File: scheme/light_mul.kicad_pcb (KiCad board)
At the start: 2 copper layers, 100 parts, among them J1 Screw_Terminal_01x04 (buttons), J2 Conn_01x06_Male (programmer), J3 Screw_Terminal_01x06 (output), J4 Conn_01x02_Male (i2c), J5 Conn_01x02_Male (Jumper), J6 Conn_01x03_Male (Indicators), J7 Screw_Terminal_01x02 (power), Q1 IRF8308M, Q2 IRF8308M, Q3 IRF8308M, SW1 SW_Push (reset), U1 L7805, U2 ATmega8A-PU

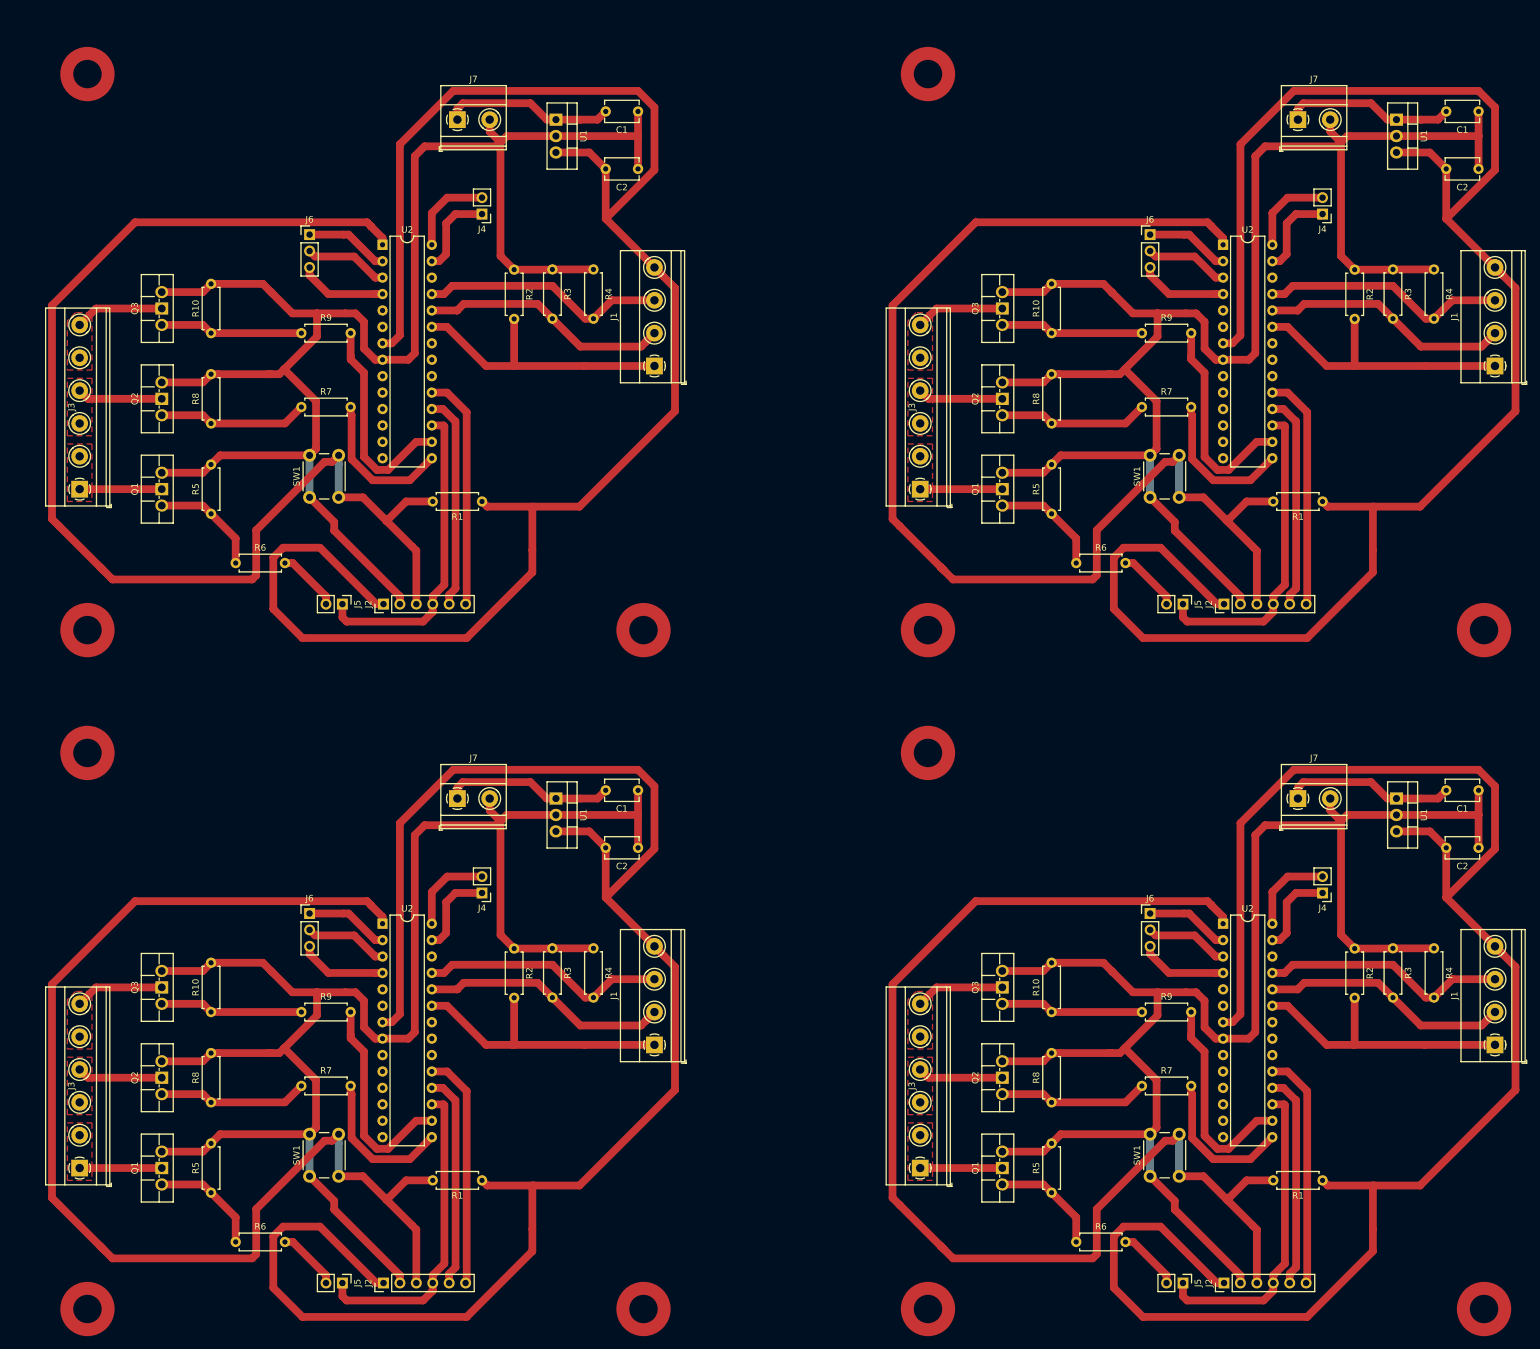
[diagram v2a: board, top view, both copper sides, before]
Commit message: cheme: add marks layer
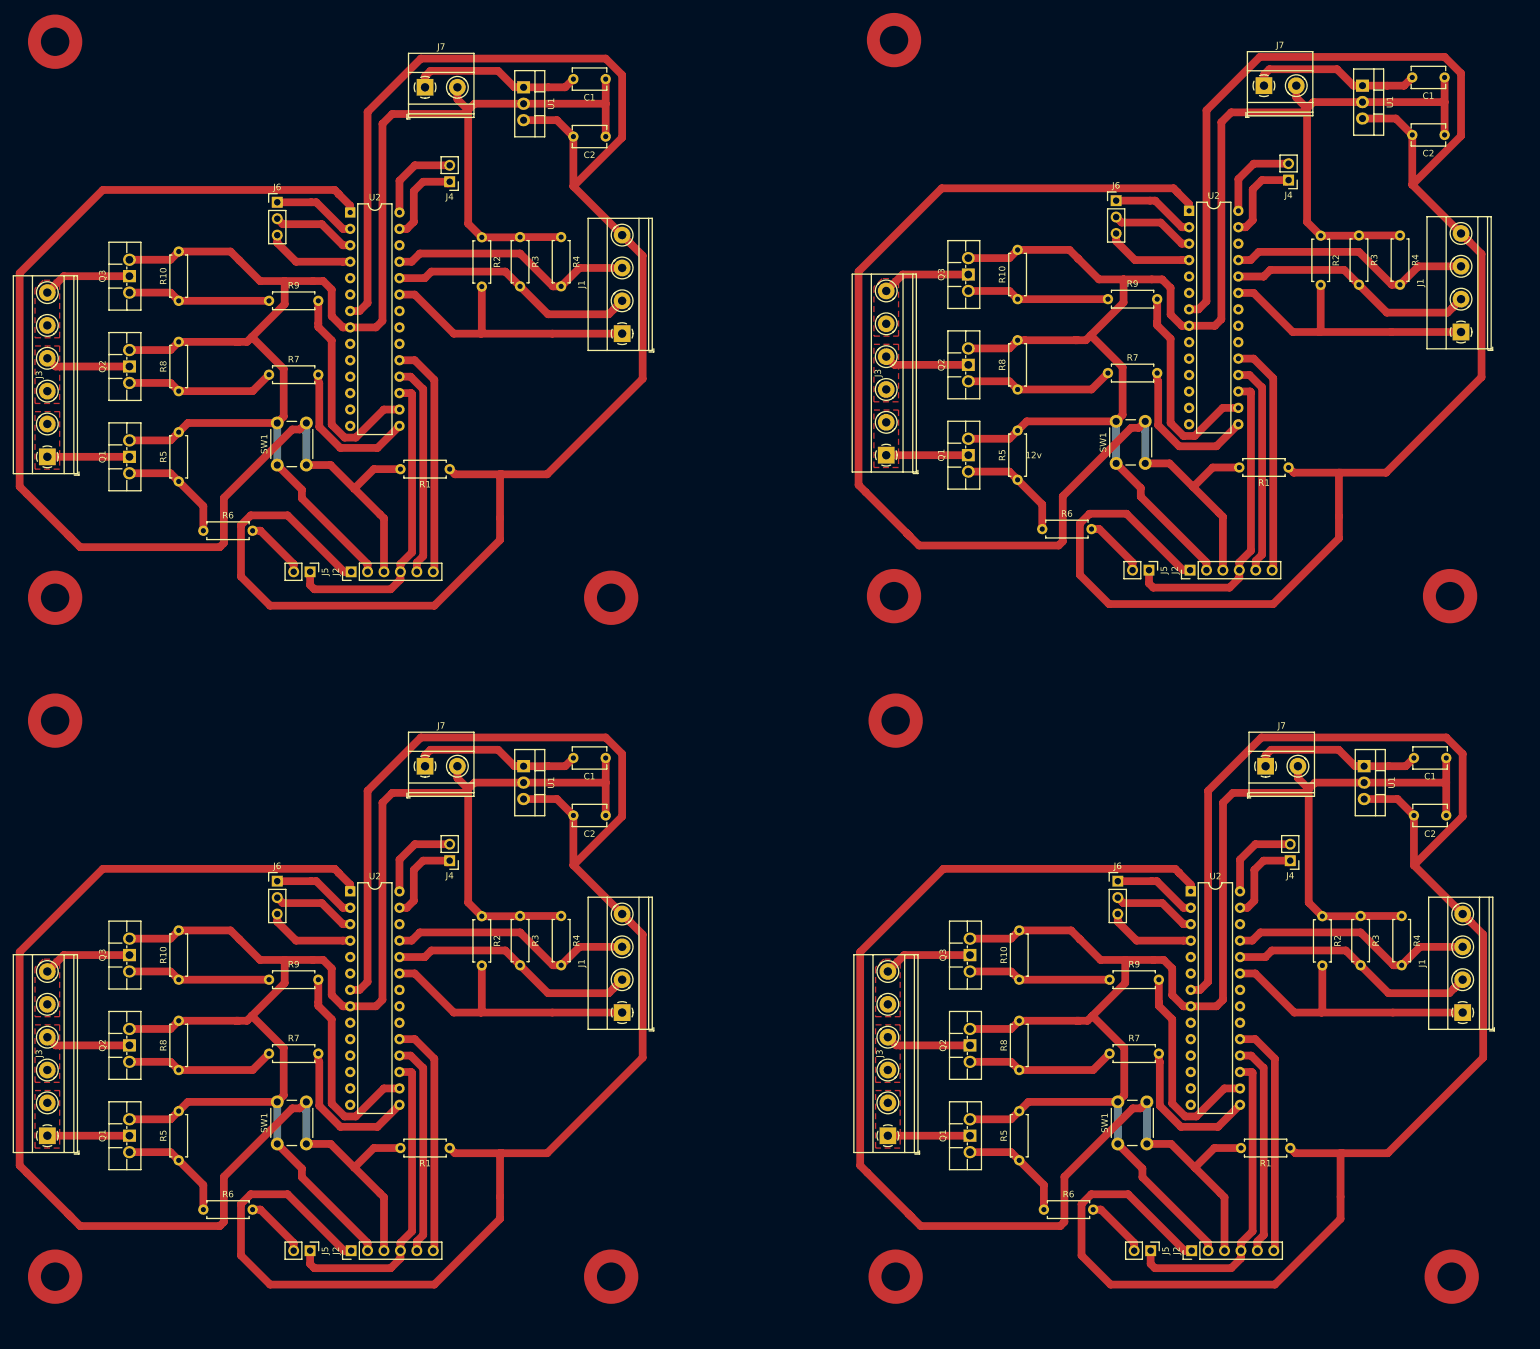
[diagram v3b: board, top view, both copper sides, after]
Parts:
- removed the C1 at (227.2, 122.8)
- removed the C1 at (227.2, 17.8)
- removed the C1 at (97.2, 122.8)
- removed the C2 at (227.2, 131.7)
- removed the C2 at (227.2, 26.7)
- removed the C2 at (97.2, 131.7)
- removed the J1 at (229.7, 162.2)
- removed the J1 at (229.7, 57.1)
- removed the J1 at (99.7, 162.2)
- removed the J2 at (187.8, 199.0)
- removed the J2 at (187.8, 94.0)
- removed the J2 at (57.8, 199.0)
- removed the J3 at (140.8, 181.2)
- removed the J3 at (140.8, 76.2)
- removed the J3 at (10.8, 181.2)
- removed the J4 at (203.0, 138.7)
- removed the J4 at (203.0, 33.7)
- removed the J4 at (73.0, 138.7)
- removed the J5 at (181.4, 199.0)
- removed the J5 at (181.4, 94.0)
- removed the J5 at (51.4, 199.0)
- removed the J6 at (176.4, 141.8)
- removed the J6 at (176.4, 36.8)
- removed the J6 at (46.4, 141.8)
- removed the J7 at (199.2, 124.0)
- removed the J7 at (199.2, 19.1)
- removed the J7 at (69.2, 124.0)
- removed the Q1 at (153.5, 183.7)
- removed the Q1 at (153.5, 78.7)
- removed the Q1 at (23.5, 183.7)
- removed the Q2 at (153.5, 169.8)
- removed the Q2 at (153.5, 64.8)
- removed the Q2 at (23.5, 169.8)
- removed the Q3 at (153.5, 155.8)
- removed the Q3 at (153.5, 50.8)
- removed the Q3 at (23.5, 155.8)
- removed the R1 at (203.0, 183.1)
- removed the R1 at (203.0, 78.1)
- removed the R1 at (73.0, 183.1)
- removed the R10 at (161.1, 157.1)
- removed the R10 at (161.1, 52.1)
- removed the R10 at (31.1, 157.1)
- removed the R2 at (208.0, 147.3)
- removed the R2 at (208.0, 42.3)
- removed the R2 at (78.0, 147.3)
- removed the R3 at (213.9, 147.2)
- removed the R3 at (213.9, 42.2)
- removed the R3 at (83.9, 147.2)
- removed the R4 at (220.3, 147.2)
- removed the R4 at (220.3, 42.2)
- removed the R4 at (90.3, 147.2)
- removed the R5 at (161.1, 185.0)
- removed the R5 at (161.1, 80.0)
- removed the R5 at (31.1, 185.0)
- removed the R6 at (164.9, 192.6)
- removed the R6 at (164.9, 87.6)
- removed the R6 at (34.9, 192.6)
- removed the R7 at (175.1, 168.5)
- removed the R7 at (175.1, 63.5)
- removed the R7 at (45.1, 168.5)
- removed the R8 at (161.1, 171.0)
- removed the R8 at (161.1, 66.0)
- removed the R8 at (31.1, 171.0)
- removed the R9 at (175.1, 157.1)
- removed the R9 at (175.1, 52.1)
- removed the R9 at (45.1, 157.1)
- removed the SW1 at (176.4, 182.5)
- removed the SW1 at (176.4, 77.5)
- removed the SW1 at (46.4, 182.5)
- removed the U1 at (214.5, 124.0)
- removed the U1 at (214.5, 19.1)
- removed the U1 at (84.5, 124.0)
- removed the U2 at (187.6, 143.4)
- removed the U2 at (187.6, 38.4)
- removed the U2 at (57.6, 143.4)
- added C1: 3.3uF, Capacitor_THT:C_Disc_D5.1mm_W3.2mm_P5.00mm, F.Cu at (222.2, 117.8)
- added C1: 3.3uF, Capacitor_THT:C_Disc_D5.1mm_W3.2mm_P5.00mm, F.Cu at (92.2, 117.8)
- added C1: 3.3uF, Capacitor_THT:C_Disc_D5.1mm_W3.2mm_P5.00mm, F.Cu at (221.9, 12.5)
- added C2: 0.1uF, Capacitor_THT:C_Disc_D5.1mm_W3.2mm_P5.00mm, F.Cu at (222.2, 126.7)
- added C2: 0.1uF, Capacitor_THT:C_Disc_D5.1mm_W3.2mm_P5.00mm, F.Cu at (92.2, 126.7)
- added C2: 0.1uF, Capacitor_THT:C_Disc_D5.1mm_W3.2mm_P5.00mm, F.Cu at (221.9, 21.4)
- added J1: Screw_Terminal_01x04 (buttons), TerminalBlock_Phoenix:TerminalBlock_Phoenix_MKDS-1,5-4-5.08_1x04_P5.08mm_Horizontal, F.Cu at (224.7, 157.2)
- added J1: Screw_Terminal_01x04 (buttons), TerminalBlock_Phoenix:TerminalBlock_Phoenix_MKDS-1,5-4-5.08_1x04_P5.08mm_Horizontal, F.Cu at (94.7, 157.2)
- added J1: Screw_Terminal_01x04 (buttons), TerminalBlock_Phoenix:TerminalBlock_Phoenix_MKDS-1,5-4-5.08_1x04_P5.08mm_Horizontal, F.Cu at (224.4, 51.9)
- added J2: Conn_01x06_Male (programmer), Connector_PinHeader_2.54mm:PinHeader_1x06_P2.54mm_Vertical, F.Cu at (182.8, 194.0)
- added J2: Conn_01x06_Male (programmer), Connector_PinHeader_2.54mm:PinHeader_1x06_P2.54mm_Vertical, F.Cu at (52.8, 194.0)
- added J2: Conn_01x06_Male (programmer), Connector_PinHeader_2.54mm:PinHeader_1x06_P2.54mm_Vertical, F.Cu at (182.5, 88.7)
- added J3: Screw_Terminal_01x06 (output), TerminalBlock_Phoenix:TerminalBlock_Phoenix_MKDS-1,5-6-5.08_1x06_P5.08mm_Horizontal, F.Cu at (135.8, 176.2)
- added J3: Screw_Terminal_01x06 (output), TerminalBlock_Phoenix:TerminalBlock_Phoenix_MKDS-1,5-6-5.08_1x06_P5.08mm_Horizontal, F.Cu at (5.79, 176.2)
- added J3: Screw_Terminal_01x06 (output), TerminalBlock_Phoenix:TerminalBlock_Phoenix_MKDS-1,5-6-5.08_1x06_P5.08mm_Horizontal, F.Cu at (135.5, 70.9)
- added J4: Conn_01x02_Male (i2c), Connector_PinHeader_2.54mm:PinHeader_1x02_P2.54mm_Vertical, F.Cu at (198.0, 133.7)
- added J4: Conn_01x02_Male (i2c), Connector_PinHeader_2.54mm:PinHeader_1x02_P2.54mm_Vertical, F.Cu at (68.0, 133.7)
- added J4: Conn_01x02_Male (i2c), Connector_PinHeader_2.54mm:PinHeader_1x02_P2.54mm_Vertical, F.Cu at (197.8, 28.4)
- added J5: Conn_01x02_Male (Jumper), Connector_PinHeader_2.54mm:PinHeader_1x02_P2.54mm_Vertical, F.Cu at (176.4, 194.0)
- added J5: Conn_01x02_Male (Jumper), Connector_PinHeader_2.54mm:PinHeader_1x02_P2.54mm_Vertical, F.Cu at (46.4, 194.0)
- added J5: Conn_01x02_Male (Jumper), Connector_PinHeader_2.54mm:PinHeader_1x02_P2.54mm_Vertical, F.Cu at (176.2, 88.7)
- added J6: Conn_01x03_Male (Indicators), Connector_PinHeader_2.54mm:PinHeader_1x03_P2.54mm_Vertical, F.Cu at (171.4, 136.8)
- added J6: Conn_01x03_Male (Indicators), Connector_PinHeader_2.54mm:PinHeader_1x03_P2.54mm_Vertical, F.Cu at (41.4, 136.8)
- added J6: Conn_01x03_Male (Indicators), Connector_PinHeader_2.54mm:PinHeader_1x03_P2.54mm_Vertical, F.Cu at (171.1, 31.6)
- added J7: Screw_Terminal_01x02 (power), TerminalBlock_Phoenix:TerminalBlock_Phoenix_MKDS-1,5-2_1x02_P5.00mm_Horizontal, F.Cu at (194.2, 119.0)
- added J7: Screw_Terminal_01x02 (power), TerminalBlock_Phoenix:TerminalBlock_Phoenix_MKDS-1,5-2_1x02_P5.00mm_Horizontal, F.Cu at (64.2, 119.0)
- added J7: Screw_Terminal_01x02 (power), TerminalBlock_Phoenix:TerminalBlock_Phoenix_MKDS-1,5-2_1x02_P5.00mm_Horizontal, F.Cu at (194.0, 13.8)
- added Q1: IRF8308M, scheme:IRF840, F.Cu at (148.5, 178.7)
- added Q1: IRF8308M, scheme:IRF840, F.Cu at (18.5, 178.7)
- added Q1: IRF8308M, scheme:IRF840, F.Cu at (148.2, 73.5)
- added Q2: IRF8308M, scheme:IRF840, F.Cu at (148.5, 164.8)
- added Q2: IRF8308M, scheme:IRF840, F.Cu at (18.5, 164.8)
- added Q2: IRF8308M, scheme:IRF840, F.Cu at (148.2, 59.5)
- added Q3: IRF8308M, scheme:IRF840, F.Cu at (148.5, 150.8)
- added Q3: IRF8308M, scheme:IRF840, F.Cu at (18.5, 150.8)
- added Q3: IRF8308M, scheme:IRF840, F.Cu at (148.2, 45.5)
- added R1: 10K, Resistor_THT:R_Axial_DIN0207_L6.3mm_D2.5mm_P7.62mm_Horizontal, F.Cu at (198.0, 178.1)
- added R1: 10K, Resistor_THT:R_Axial_DIN0207_L6.3mm_D2.5mm_P7.62mm_Horizontal, F.Cu at (68.0, 178.1)
- added R1: 10K, Resistor_THT:R_Axial_DIN0207_L6.3mm_D2.5mm_P7.62mm_Horizontal, F.Cu at (197.8, 72.9)
- added R10: 10K, Resistor_THT:R_Axial_DIN0207_L6.3mm_D2.5mm_P7.62mm_Horizontal, F.Cu at (156.1, 152.1)
- added R10: 10K, Resistor_THT:R_Axial_DIN0207_L6.3mm_D2.5mm_P7.62mm_Horizontal, F.Cu at (26.1, 152.1)
- added R10: 10K, Resistor_THT:R_Axial_DIN0207_L6.3mm_D2.5mm_P7.62mm_Horizontal, F.Cu at (155.9, 46.8)
- added R2: 220Ohm, Resistor_THT:R_Axial_DIN0207_L6.3mm_D2.5mm_P7.62mm_Horizontal, F.Cu at (203.0, 142.3)
- added R2: 220Ohm, Resistor_THT:R_Axial_DIN0207_L6.3mm_D2.5mm_P7.62mm_Horizontal, F.Cu at (73.0, 142.3)
- added R2: 220Ohm, Resistor_THT:R_Axial_DIN0207_L6.3mm_D2.5mm_P7.62mm_Horizontal, F.Cu at (202.7, 37.0)
- added R3: 220Ohm, Resistor_THT:R_Axial_DIN0207_L6.3mm_D2.5mm_P7.62mm_Horizontal, F.Cu at (208.9, 142.2)
- added R3: 220Ohm, Resistor_THT:R_Axial_DIN0207_L6.3mm_D2.5mm_P7.62mm_Horizontal, F.Cu at (78.9, 142.2)
- added R3: 220Ohm, Resistor_THT:R_Axial_DIN0207_L6.3mm_D2.5mm_P7.62mm_Horizontal, F.Cu at (208.7, 37.0)
- added R4: 220Ohm, Resistor_THT:R_Axial_DIN0207_L6.3mm_D2.5mm_P7.62mm_Horizontal, F.Cu at (215.3, 142.2)
- added R4: 220Ohm, Resistor_THT:R_Axial_DIN0207_L6.3mm_D2.5mm_P7.62mm_Horizontal, F.Cu at (85.3, 142.2)
- added R4: 220Ohm, Resistor_THT:R_Axial_DIN0207_L6.3mm_D2.5mm_P7.62mm_Horizontal, F.Cu at (215.0, 37.0)
- added R5: 10K, Resistor_THT:R_Axial_DIN0207_L6.3mm_D2.5mm_P7.62mm_Horizontal, F.Cu at (156.1, 180.0)
- added R5: 10K, Resistor_THT:R_Axial_DIN0207_L6.3mm_D2.5mm_P7.62mm_Horizontal, F.Cu at (26.1, 180.0)
- added R5: 10K, Resistor_THT:R_Axial_DIN0207_L6.3mm_D2.5mm_P7.62mm_Horizontal, F.Cu at (155.9, 74.8)
- added R6: 100Ohm, Resistor_THT:R_Axial_DIN0207_L6.3mm_D2.5mm_P7.62mm_Horizontal, F.Cu at (159.9, 187.6)
- added R6: 100Ohm, Resistor_THT:R_Axial_DIN0207_L6.3mm_D2.5mm_P7.62mm_Horizontal, F.Cu at (29.9, 187.6)
- added R6: 100Ohm, Resistor_THT:R_Axial_DIN0207_L6.3mm_D2.5mm_P7.62mm_Horizontal, F.Cu at (159.7, 82.4)
- added R7: 100Ohm, Resistor_THT:R_Axial_DIN0207_L6.3mm_D2.5mm_P7.62mm_Horizontal, F.Cu at (170.1, 163.5)
- added R7: 100Ohm, Resistor_THT:R_Axial_DIN0207_L6.3mm_D2.5mm_P7.62mm_Horizontal, F.Cu at (40.1, 163.5)
- added R7: 100Ohm, Resistor_THT:R_Axial_DIN0207_L6.3mm_D2.5mm_P7.62mm_Horizontal, F.Cu at (169.8, 58.2)
- added R8: 10K, Resistor_THT:R_Axial_DIN0207_L6.3mm_D2.5mm_P7.62mm_Horizontal, F.Cu at (156.1, 166.0)
- added R8: 10K, Resistor_THT:R_Axial_DIN0207_L6.3mm_D2.5mm_P7.62mm_Horizontal, F.Cu at (26.1, 166.0)
- added R8: 10K, Resistor_THT:R_Axial_DIN0207_L6.3mm_D2.5mm_P7.62mm_Horizontal, F.Cu at (155.9, 60.8)
- added R9: 100Ohm, Resistor_THT:R_Axial_DIN0207_L6.3mm_D2.5mm_P7.62mm_Horizontal, F.Cu at (170.1, 152.1)
- added R9: 100Ohm, Resistor_THT:R_Axial_DIN0207_L6.3mm_D2.5mm_P7.62mm_Horizontal, F.Cu at (40.1, 152.1)
- added R9: 100Ohm, Resistor_THT:R_Axial_DIN0207_L6.3mm_D2.5mm_P7.62mm_Horizontal, F.Cu at (169.8, 46.8)
- added SW1: SW_Push (reset), Button_Switch_THT:SW_PUSH_6mm, F.Cu at (171.4, 177.5)
- added SW1: SW_Push (reset), Button_Switch_THT:SW_PUSH_6mm, F.Cu at (41.4, 177.5)
- added SW1: SW_Push (reset), Button_Switch_THT:SW_PUSH_6mm, F.Cu at (171.1, 72.2)
- added U1: L7805, Package_TO_SOT_THT:TO-220-3_Vertical, F.Cu at (209.5, 119.0)
- added U1: L7805, Package_TO_SOT_THT:TO-220-3_Vertical, F.Cu at (79.5, 119.0)
- added U1: L7805, Package_TO_SOT_THT:TO-220-3_Vertical, F.Cu at (209.2, 13.8)
- added U2: ATmega8A-PU, Package_DIP:DIP-28_W7.62mm, F.Cu at (182.6, 138.4)
- added U2: ATmega8A-PU, Package_DIP:DIP-28_W7.62mm, F.Cu at (52.6, 138.4)
- added U2: ATmega8A-PU, Package_DIP:DIP-28_W7.62mm, F.Cu at (182.4, 33.2)
- moved R8 7.07 mm to (26.1, 61.0)
- moved C1 7.07 mm to (92.2, 12.8)
- moved C2 7.07 mm to (92.2, 21.7)
- moved J1 7.07 mm to (94.7, 52.1)
- moved J2 7.07 mm to (52.8, 89.0)
- moved J3 7.07 mm to (5.79, 71.2)
- moved J4 7.07 mm to (68.0, 28.7)
- moved J5 7.07 mm to (46.4, 89.0)
- moved J6 7.07 mm to (41.4, 31.8)
- moved J7 7.07 mm to (64.2, 14.1)
- moved Q1 7.07 mm to (18.5, 73.7)
- moved Q3 7.07 mm to (18.5, 45.8)
- moved R1 7.07 mm to (68.0, 73.1)
- moved R10 7.07 mm to (26.1, 47.1)
- moved R2 7.07 mm to (73.0, 37.3)
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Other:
- board text added: "+"
- board text added: "-"
- board text added: "1"
- board text added: "100Ohm"
- board text added: "10kOhm"
- board text added: "12v"
- board text added: "2"
- board text added: "220Ohm"
- board text added: "3"
- board text added: "5v +"
- board text added: "Buttons"
- board text added: "GND"
- board text added: "Info OUT"
- board text added: "Jumper"
- board text added: "MISO"
- board text added: "MOSI"
- board text added: "Max 40v, Max 30 A"
- board text added: "Normally: ON Programmer: OFF"
- board text added: "Pwr OUT"
- board text added: "Reset"
- board text added: "SCK"
- board text added: "SCL"
- board text added: "SDA"
- board text added: "TWP"
